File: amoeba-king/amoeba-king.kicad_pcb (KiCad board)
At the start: 2 copper layers, 19 x 19.1 mm, 14 parts, among them J1 Conn_01x04_Male, J2 Conn_01x04_Male, J3 Conn_01x04_Male, J4 Conn_01x04_Male, J5 Conn_01x01_Male, J6 Conn_01x01_Male

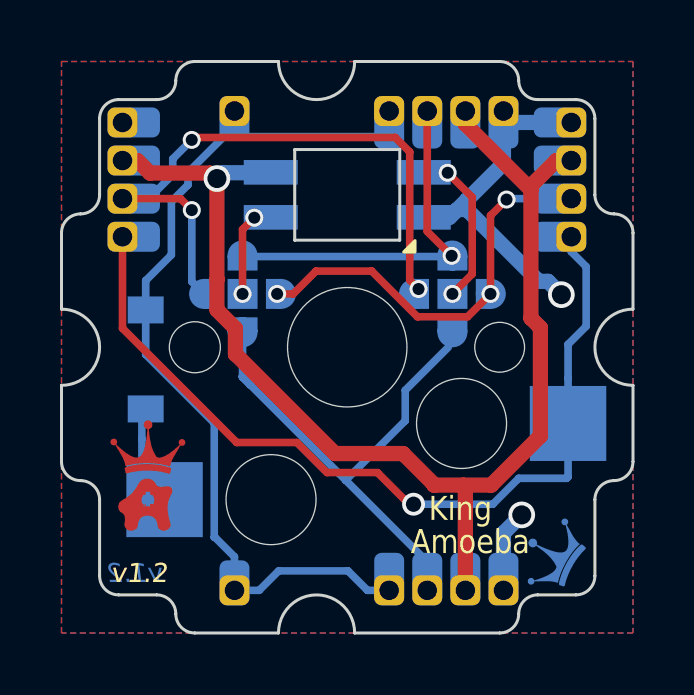
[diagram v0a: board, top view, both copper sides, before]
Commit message: Rounded tracks, and gerber file.
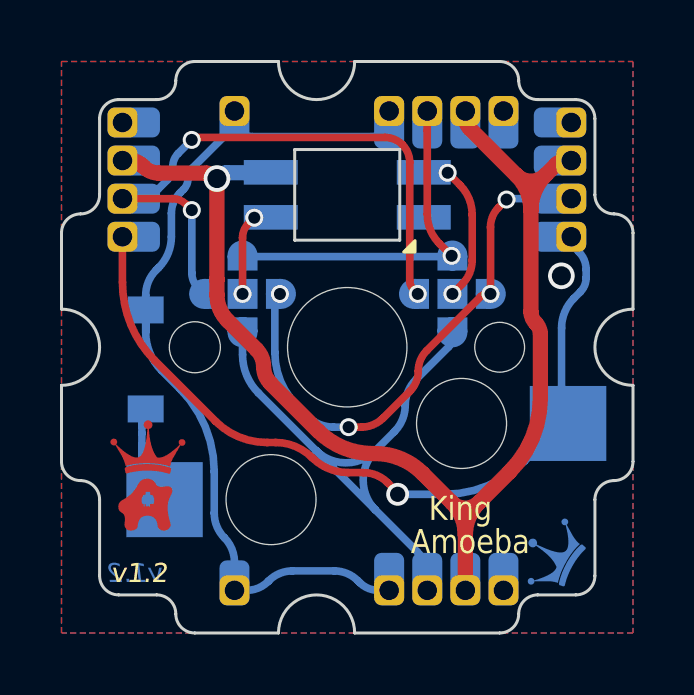
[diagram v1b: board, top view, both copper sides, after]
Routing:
- net /GND: track 14.5 -> 0.25 mm, vias 2 -> 1
- net Net-(J1-Pad2): track 13.9 -> 18.3 mm, vias 3 -> 4
- net /R: track 29.2 -> 25.9 mm
- net /VDD: track 41.3 -> 43.5 mm
- net Net-(J4-Pad2): track 18.6 -> 20.4 mm

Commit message: Moved some graphics for better legibility.
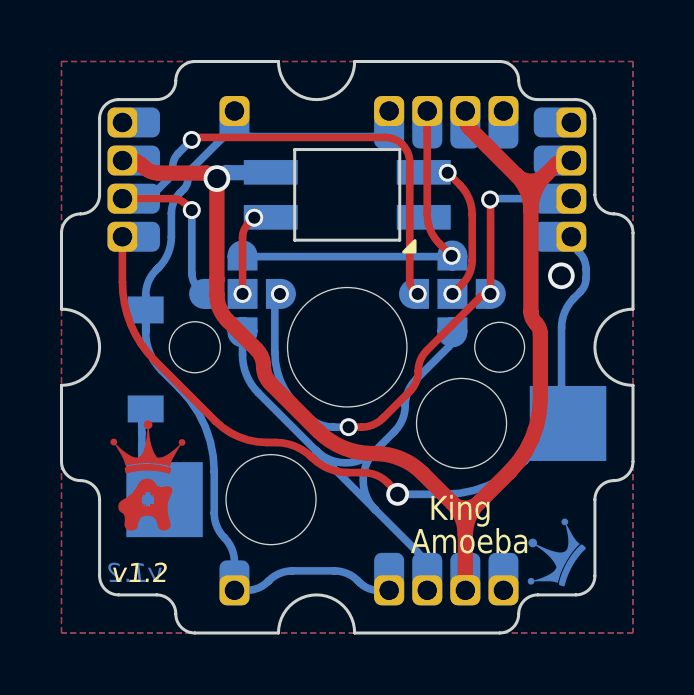
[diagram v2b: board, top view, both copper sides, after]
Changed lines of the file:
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@@
     )
     (fp_line (start 0.8128 -1.28) (end 0.8128 -0.8128) (layer "B.SilkS") (width 0.12))
-    (fp_line (start -1.21778 -0.97902) (end -1.51778 -1.27902) (layer "B.SilkS") (width 0.12))
     (fp_line (start -0.8128 -0.8128) (end -0.8128 -1.28) (layer "B.SilkS") (width 0.12))
     (fp_line (start -0.8128 0.8128) (end -1.28 0.8128) (layer "B.SilkS") (width 0.12))
@@
     (fp_line (start 0.8128 -0.8128) (end 1.28 -0.8128) (layer "B.SilkS") (width 0.12))
     (fp_line (start -0.8128 1.28) (end -0.8128 0.8128) (layer "B.SilkS") (width 0.12))
-    (fp_line (start -1.51778 -1.27902) (end -0.91778 -1.27902) (layer "B.SilkS") (width 0.12))
     (fp_line (start 1.28 0.8128) (end 0.8128 0.8128) (layer "B.SilkS") (width 0.12))
-    (fp_line (start -1.21778 -0.97902) (end -0.91778 -1.27902) (layer "B.SilkS") (width 0.12))
     (fp_line (start -1.28 -0.8128) (end -0.8128 -0.8128) (layer "B.SilkS") (width 0.12))
     (fp_arc (start -0.8128 -1.28) (mid 0 -2.0928) (end 0.8128 -1.28) (layer "B.SilkS") (width 0.12))
@@
       (effects (font (size 1 1) (thickness 0.15)) (justify mirror))
     )
-    (fp_line (start -1.51778 -1.27902) (end -0.91778 -1.27902) (layer "B.SilkS") (width 0.12))
     (fp_line (start 0.8128 -1.28) (end 0.8128 -0.8128) (layer "B.SilkS") (width 0.12))
     (fp_line (start 0.8128 0.8128) (end 0.8128 1.28) (layer "B.SilkS") (width 0.12))
-    (fp_line (start -1.21778 -0.97902) (end -1.51778 -1.27902) (layer "B.SilkS") (width 0.12))
     (fp_line (start -0.8128 -0.8128) (end -0.8128 -1.28) (layer "B.SilkS") (width 0.12))
-    (fp_line (start -1.21778 -0.97902) (end -0.91778 -1.27902) (layer "B.SilkS") (width 0.12))
     (fp_line (start -0.8128 0.8128) (end -1.28 0.8128) (layer "B.SilkS") (width 0.12))
     (fp_line (start 1.28 0.8128) (end 0.8128 0.8128) (layer "B.SilkS") (width 0.12))
@@
     (effects (font (size 0.635 0.635) (thickness 0.15875) italic) (justify mirror))
   )
-  (gr_text "D" (at 69.4436 163.703) (layer "B.SilkS")
+  (gr_text "D" (at 69.6 163.703) (layer "B.SilkS")
     (effects (font (size 0.762 0.762) (thickness 0.1524)) (justify mirror))
   )
-  (gr_text "R" (at 81.5594 165.0238) (layer "B.SilkS")
+  (gr_text "R" (at 81.2 165.0238) (layer "B.SilkS")
     (effects (font (size 0.762 0.762) (thickness 0.15)) (justify mirror))
   )
@@
     (effects (font (size 0.762 0.762) (thickness 0.1524)) (justify mirror))
   )
-  (gr_text "V" (at 81.5594 162.4838) (layer "B.SilkS")
+  (gr_text "V" (at 81.2 162.4838) (layer "B.SilkS")
     (effects (font (size 0.762 0.762) (thickness 0.1524)) (justify mirror))
   )
-  (gr_text "D" (at 81.4832 163.7792) (layer "B.SilkS")
+  (gr_text "D" (at 81.2 163.7792) (layer "B.SilkS")
     (effects (font (size 0.762 0.762) (thickness 0.1524)) (justify mirror))
   )
@@
     (effects (font (size 0.762 0.762) (thickness 0.1524)) (justify mirror))
   )
-  (gr_text "V" (at 69.4182 162.433) (layer "B.SilkS")
+  (gr_text "V" (at 69.6 162.433) (layer "B.SilkS")
     (effects (font (size 0.762 0.762) (thickness 0.1524)) (justify mirror))
   )
@@
     (effects (font (size 0.6096 0.6096) (thickness 0.127)) (justify mirror))
   )
-  (gr_text "R" (at 69.4182 165.0238) (layer "B.SilkS")
+  (gr_text "R" (at 69.6 165.0238) (layer "B.SilkS")
     (effects (font (size 0.762 0.762) (thickness 0.15)) (justify mirror))
   )
@@
     (effects (font (size 0.762 0.762) (thickness 0.1524)) (justify mirror))
   )
-  (gr_text "G" (at 69.4182 161.2138) (layer "B.SilkS")
+  (gr_text "G" (at 69.6 161.2138) (layer "B.SilkS")
     (effects (font (size 0.762 0.762) (thickness 0.1524)) (justify mirror))
   )
@@
   (arc (start 79.6036 165.750626) (mid 79.517783 166.182053) (end 79.2734 166.5478) (width 0.254) (layer "F.Cu") (net 1))
   (segment (start 77.524457 170.125542) (end 76.630979 171.01902) (width 0.254) (layer "F.Cu") (net 2))
-  (segment (start 80.480211 164.000089) (end 80.747222 163.733078) (width 0.254) (layer "F.Cu") (net 2))
   (segment (start 79.895182 166.961067) (end 78.085723 168.770525) (width 0.254) (layer "F.Cu") (net 2))
   (segment (start 75.907112 171.318856) (end 75.483081 171.318856) (width 0.254) (layer "F.Cu") (net 2))
-  (segment (start 80.2132 164.64471) (end 80.2132 166.878) (width 0.254) (layer "F.Cu") (net 2))
+  (segment (start 80.2132 166.878) (end 80.2132 163.746278) (width 0.254) (layer "F.Cu") (net 2))
+  (segment (start 80.2132 163.746278) (end 80.2 163.733078) (width 0.254) (layer "F.Cu") (net 2))
   (segment (start 80.095725 166.878) (end 80.2132 166.878) (width 0.254) (layer "F.Cu") (net 2))
   (via (at 80.2132 166.878) (size 0.6) (drill 0.4) (layers "F.Cu" "B.Cu") (net 2))
   (via (at 75.483081 171.318856) (size 0.6) (drill 0.4) (layers "F.Cu" "B.Cu") (free) (net 2))
-  (via (at 80.747222 163.733078) (size 0.6) (drill 0.4) (layers "F.Cu" "B.Cu") (net 2))
+  (via (at 80.2 163.733078) (size 0.6) (drill 0.4) (layers "F.Cu" "B.Cu") (net 2))
   (via (at 73.193773 166.880716) (size 0.6) (drill 0.4) (layers "F.Cu" "B.Cu") (net 2))
-  (arc (start 80.480211 164.000089) (mid 80.282593 164.295843) (end 80.2132 164.64471) (width 0.254) (layer "F.Cu") (net 2))
   (arc (start 77.805091 169.448034) (mid 77.878024 169.081369) (end 78.085723 168.770525) (width 0.254) (layer "F.Cu") (net 2))
   (arc (start 75.907112 171.318856) (mid 76.298866 171.240931) (end 76.630979 171.01902) (width 0.254) (layer "F.Cu") (net 2))
@@
   (segment (start 73.753178 170.590678) (end 74.127192 170.964692) (width 0.254) (layer "B.Cu") (net 2))
   (segment (start 75.483081 171.318856) (end 74.982218 171.318856) (width 0.254) (layer "B.Cu") (net 2))
-  (segment (start 80.7773 163.703) (end 82.9056 163.703) (width 0.254) (layer "B.Cu") (net 2))
+  (segment (start 80.230078 163.703) (end 80.2 163.733078) (width 0.254) (layer "B.Cu") (net 2))
   (segment (start 73.025 168.8327) (end 73.025 167.223518) (width 0.254) (layer "B.Cu") (net 2))
+  (segment (start 82.9056 163.703) (end 80.230078 163.703) (width 0.254) (layer "B.Cu") (net 2))
   (segment (start 73.1262 166.9792) (end 73.2274 166.878) (width 0.254) (layer "B.Cu") (net 2))
   (arc (start 73.025 167.223518) (mid 73.051301 167.091294) (end 73.1262 166.9792) (width 0.254) (layer "B.Cu") (net 2))

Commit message: Added row via to be used as an anchor point for cabling.
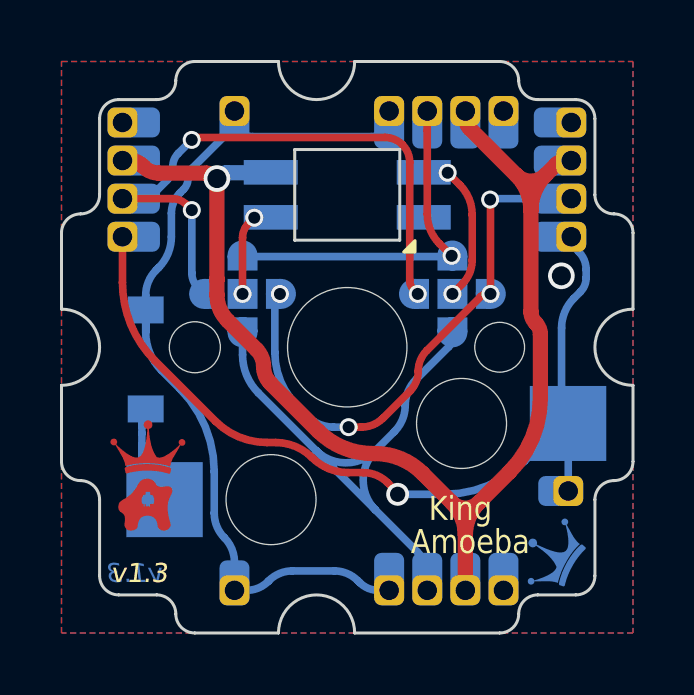
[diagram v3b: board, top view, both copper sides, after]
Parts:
- added J7: Conn_01x01_Male, amoeba-modules:Header_1x01_P1.27mm, B.Cu at (82.8, 173.4)
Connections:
- JP2 pad 2: /DOUT -> /R
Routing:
- net /R: track 25.9 -> 28.1 mm
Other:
- board text added: "v1.3"
- board text removed: "v1.2"
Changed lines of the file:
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@@
     )
     (pad_to_mask_clearance 0)
+    (grid_origin 82.804 173.447031)
     (pcbplotparams
       (layerselection 0x00010f0_ffffffff)
@@
   (footprint "amoeba-modules:Kailh_MX_Socket" (layer "B.Cu")
     (at 75.438 168.656)
-    (property "Sheetfile" "switch.kicad_sch")
+    (property "Sheetfile" "File: switch.kicad_sch")
     (property "Sheetname" "switch")
     (attr through_hole)
@@
     (descr "Through hole straight pin header, 1x04, 1.27mm pitch, single row")
     (tags "Through hole pin header THT 1x04 1.27mm single row")
-    (property "Sheetfile" "/Users/climent/Sources/amoeba-king/amoeba-king/amoeba-king.sch")
+    (property "Sheetfile" "File: amoeba-king.kicad_sch")
     (property "Sheetname" "")
     (attr through_hole)
@@
     (descr "Through hole straight pin header, 1x04, 1.27mm pitch, single row")
     (tags "Through hole pin header THT 1x04 1.27mm single row")
-    (property "Sheetfile" "/Users/climent/Sources/amoeba-king/amoeba-king/amoeba-king.sch")
+    (property "Sheetfile" "File: amoeba-king.kicad_sch")
     (property "Sheetname" "")
     (attr through_hole)
@@
     (descr "SMD Solder 3-pad Jumper, 1x1.5mm rounded Pads, 0.3mm gap, open")
     (tags "solder jumper open")
-    (property "Sheetfile" "/Users/climent/Sources/amoeba-king/amoeba-king/amoeba-king.sch")
+    (property "Sheetfile" "File: amoeba-king.kicad_sch")
     (property "Sheetname" "")
     (attr exclude_from_pos_files)
@@
       ))
     (pad "2" smd rect (at 0 0 180) (size 1 1) (layers "B.Cu" "B.Mask")
-      (net 3 "/DOUT") (pinfunction "C") (pintype "input"))
+      (net 6 "/R") (pinfunction "C") (pintype "input"))
     (pad "3" smd custom (at 1.28 0 180) (size 0.5 0.5) (layers "B.Cu" "B.Mask")
       (net 8 "Net-(J3-Pad2)") (pinfunction "B") (pintype "passive") (zone_connect 2)
@@
     (descr "Through hole straight pin header, 1x01, 1.27mm pitch, single row")
     (tags "Through hole pin header THT 1x01 1.27mm single row")
-    (property "Sheetfile" "/Users/climent/Sources/amoeba-king/amoeba-king/amoeba-king.sch")
+    (property "Sheetfile" "File: amoeba-king.kicad_sch")
     (property "Sheetname" "")
     (attr through_hole)
@@
     (descr "Through hole straight pin header, 1x01, 1.27mm pitch, single row")
     (tags "Through hole pin header THT 1x01 1.27mm single row")
-    (property "Sheetfile" "/Users/climent/Sources/amoeba-king/amoeba-king/amoeba-king.sch")
+    (property "Sheetfile" "File: amoeba-king.kicad_sch")
     (property "Sheetname" "")
     (attr through_hole)
@@
     (descr "SMD Solder 3-pad Jumper, 1x1.5mm rounded Pads, 0.3mm gap, open")
     (tags "solder jumper open")
-    (property "Sheetfile" "/Users/climent/Sources/amoeba-king/amoeba-king/amoeba-king.sch")
+    (property "Sheetfile" "File: amoeba-king.kicad_sch")
     (property "Sheetname" "")
     (attr exclude_from_pos_files)
@@
     (descr "Through hole straight pin header, 1x04, 1.27mm pitch, single row")
     (tags "Through hole pin header THT 1x04 1.27mm single row")
-    (property "Sheetfile" "/Users/climent/Sources/amoeba-king/amoeba-king/amoeba-king.sch")
+    (property "Sheetfile" "File: amoeba-king.kicad_sch")
     (property "Sheetname" "")
     (attr through_hole)
@@
     (descr "SOD-123")
     (tags "SOD-123")
-    (property "Sheetfile" "switch.kicad_sch")
+    (property "Sheetfile" "File: switch.kicad_sch")
     (property "Sheetname" "switch")
     (attr smd)
@@
     (descr "Through hole straight pin header, 1x04, 1.27mm pitch, single row")
     (tags "Through hole pin header THT 1x04 1.27mm single row")
-    (property "Sheetfile" "/Users/climent/Sources/amoeba-king/amoeba-king/amoeba-king.sch")
+    (property "Sheetfile" "File: amoeba-king.kicad_sch")
     (property "Sheetname" "")
     (attr through_hole)
@@
   (footprint "amoeba-modules:LED_SK6812MINI_E_PLCC4_3.2x2.8mm_Shine_Through" (layer "B.Cu")
     (at 75.438 163.576 180)
-    (property "Sheetfile" "led.kicad_sch")
+    (property "Sheetfile" "File: led.kicad_sch")
     (property "Sheetname" "led")
     (attr through_hole)
@@
       (net 1 "/DIN") (pinfunction "DIN") (pintype "input"))
   )
+  (footprint "amoeba-modules:Header_1x01_P1.27mm" (layer "B.Cu")
+    (at 82.804 173.447031 180)
+    (descr "Through hole straight pin header, 1x01, 1.27mm pitch, single row")
+    (tags "Through hole pin header THT 1x01 1.27mm single row")
+    (property "Sheetfile" "File: amoeba-king.kicad_sch")
+    (property "Sheetname" "")
+    (attr through_hole)
+    (fp_text reference "J7" (at 0 1.695) (layer "B.SilkS") hide
+      (effects (font (size 1 1) (thickness 0.15)) (justify mirror))
+    )
+    (fp_text value "Conn_01x01_Male" (at 0 -1.695) (layer "B.Fab")
+      (effects (font (size 1 1) (thickness 0.15)) (justify mirror))
+    )
+    (fp_text user "${REFERENCE}" (at -2.2 -0.05 90) (layer "B.Fab")
+      (effects (font (size 1 1) (thickness 0.15)) (justify mirror))
+    )
+    (pad "1" smd roundrect locked (at 0 0 180) (size 1.5 1) (drill (offset 0.25 0)) (layers "B.Cu" "B.Paste" "B.Mask") (roundrect_rratio 0.25)
+      (net 6 "/R") (pinfunction "Pin_1") (pintype "passive"))
+    (pad "1" thru_hole roundrect locked (at 0 0 180) (size 1 1) (drill 0.65) (layers *.Cu *.Mask) (roundrect_rratio 0.25)
+      (net 6 "/R") (pinfunction "Pin_1") (pintype "passive"))
+  )
   (gr_poly
     (pts
@@
   (gr_arc (start 69.088 176.911) (mid 69.537013 177.096987) (end 69.723 177.546) (layer "Edge.Cuts") (width 0.1))
   (gr_arc (start 83.693 173.736) (mid 83.878987 173.286987) (end 84.328 173.101) (layer "Edge.Cuts") (width 0.1))
-  (gr_text "v1.2" (at 68.5038 176.1871) (layer "F.Cu")
+  (gr_text "v1.3" (at 68.5038 176.1871) (layer "F.Cu")
     (effects (font (size 0.635 0.635) (thickness 0.15875) italic))
   )
-  (gr_text "v1.2" (at 68.3895 176.1871) (layer "B.Cu")
+  (gr_text "v1.3" (at 68.3895 176.1871) (layer "B.Cu")
     (effects (font (size 0.635 0.635) (thickness 0.15875) italic) (justify mirror))
   )
-  (gr_text "v1.2" (at 68.3895 176.1871) (layer "B.SilkS")
+  (gr_text "v1.3" (at 68.3895 176.1871) (layer "B.SilkS")
     (effects (font (size 0.635 0.635) (thickness 0.15875) italic) (justify mirror))
   )
@@
     (effects (font (size 0.762 0.762) (thickness 0.15)) (justify mirror))
   )
+  (gr_text "R" (at 80.962273 173.454512) (layer "B.SilkS")
+    (effects (font (size 0.762 0.762) (thickness 0.15)) (justify mirror))
+  )
   (gr_text "Amoeba" (at 72.1614 171.5643) (layer "B.SilkS")
     (effects (font (size 0.8 0.7) (thickness 0.15)) (justify right mirror))
@@
     (effects (font (size 0.8 0.7) (thickness 0.15)))
   )
-  (gr_text "v1.2" (at 68.5038 176.1871) (layer "F.SilkS")
+  (gr_text "v1.3" (at 68.5038 176.1871) (layer "F.SilkS")
     (effects (font (size 0.635 0.635) (thickness 0.15875) italic))
   )
@@
   (arc (start 77.1174 173.530583) (mid 77.112361 173.505252) (end 77.098013 173.483779) (width 0.254) (layer "F.Cu") (net 6))
   (segment (start 82.689875 171.087875) (end 82.798 171.196) (width 0.254) (layer "B.Cu") (net 6))
+  (segment (start 82.804 171.202) (end 82.798 171.196) (width 0.254) (layer "B.Cu") (net 6))
   (segment (start 81.347755 172.453014) (end 81.802036 171.998732) (width 0.254) (layer "B.Cu") (net 6))
+  (segment (start 82.804 173.447031) (end 82.804 171.202) (width 0.254) (layer "B.Cu") (net 6))
   (segment (start 82.991325 167.026259) (end 83.207097 166.810486) (width 0.254) (layer "B.Cu") (net 6))
   (segment (start 83.15325 165.47065) (end 82.993988 165.311388) (width 0.254) (layer "B.Cu") (net 6))
